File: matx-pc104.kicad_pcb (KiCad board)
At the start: 2 copper layers, 171.4 x 243.8 mm, 100 parts, among them J1 ATX-24, J10 RST_IN, J11 Fan1, J12 Fan2, J13 Fan3, J14 VGA, J15 VGA, J16 VGA_DDC, J17 Ethernet, J18 Ethernet, J19 Keyboard, J2 PC104-8, J20 Keyboard, J21 Mouse, J22 Mouse, J23 USB, J24 USB, J25 Serial, J26 Serial, J3 PC104-16, J4 Bus_ISA_16bit, J5 Bus_ISA_16bit, J6 Bus_ISA_16bit, J7 Bus_ISA_16bit, J8 F_PANEL, J9 HDD_IN, Q1 2N7000, Q2 2N7000, SW1 Power, SW2 Reset, U1 L7905, U2 555, U3 74HCT138, U4 74HCT688, U5 74HCT574, U6 ATF16V8C, U7 4047, U8 DC56-11GWA

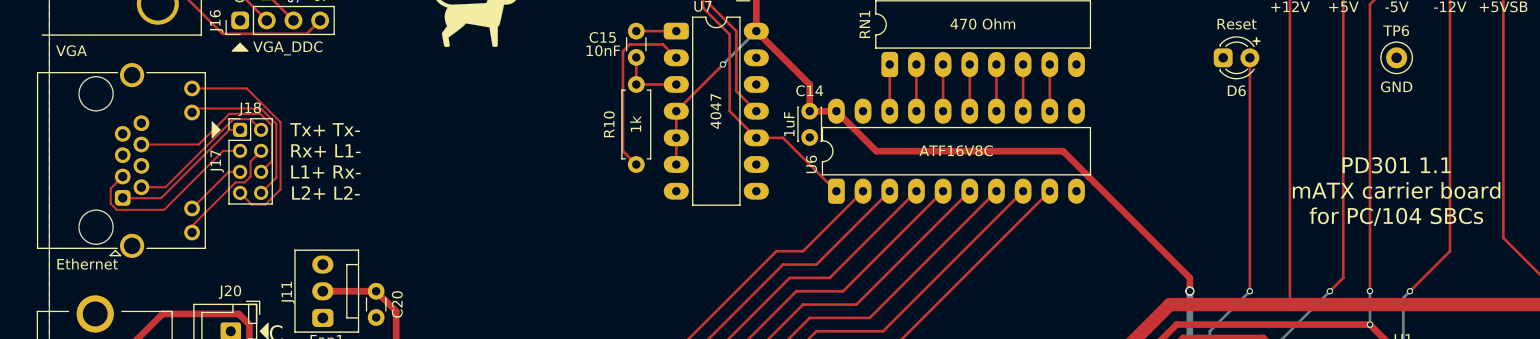
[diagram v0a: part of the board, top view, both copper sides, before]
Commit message: Adjust backpanel design for better fit
Move Ethernet jack to be flush through backpanel, make per-port cutouts for USB
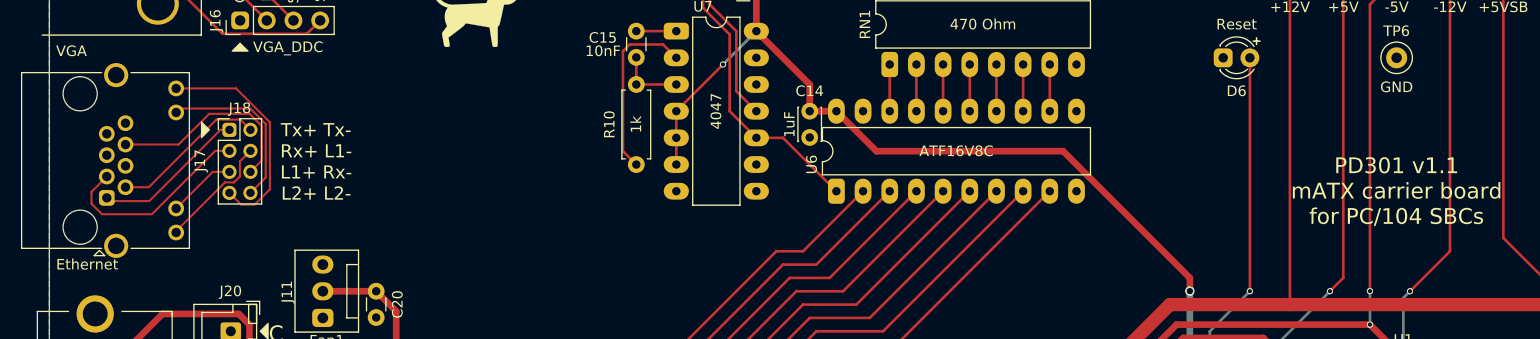
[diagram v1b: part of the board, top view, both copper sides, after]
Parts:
- moved J17 1.52 mm to (20.7, 67.9)
- moved J18 1.02 mm to (32.4, 61.5)
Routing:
- net /E_RX+: track 18.0 -> 19.2 mm
- net /E_TX+: track 13.9 -> 14.6 mm
- net /E_L2-: track 16.0 -> 16.5 mm
- net /E_RX-: track 19.0 -> 19.5 mm
- net /E_L2+: track 21.1 -> 21.6 mm
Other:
- board text added: "PD301 v1.1 mATX carrier board for PC/104 SBCs"

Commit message: Add jumper to link keyboard & mouse power
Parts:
- added JP2: K_5V=M_5V, Connector_PinHeader_2.54mm:PinHeader_1x02_P2.54mm_Vertical, F.Cu at (31.2, 96.3)
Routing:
- net /K_5V: track 24.9 -> 31.0 mm
- net /M_5V: track 24.9 -> 28.9 mm
- net -12V: track 369.3 -> 371.1 mm, vias 3 -> 4
- net +5V: track 1278.3 -> 1277.4 mm, vias 31 -> 30
- net -5V: track 324.9 -> 325.6 mm
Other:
- board text added: "Short JP2 for combo key+mouse"
